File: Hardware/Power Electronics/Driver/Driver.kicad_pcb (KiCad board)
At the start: 2 copper layers, 201.5 x 165.9 mm, 48 parts

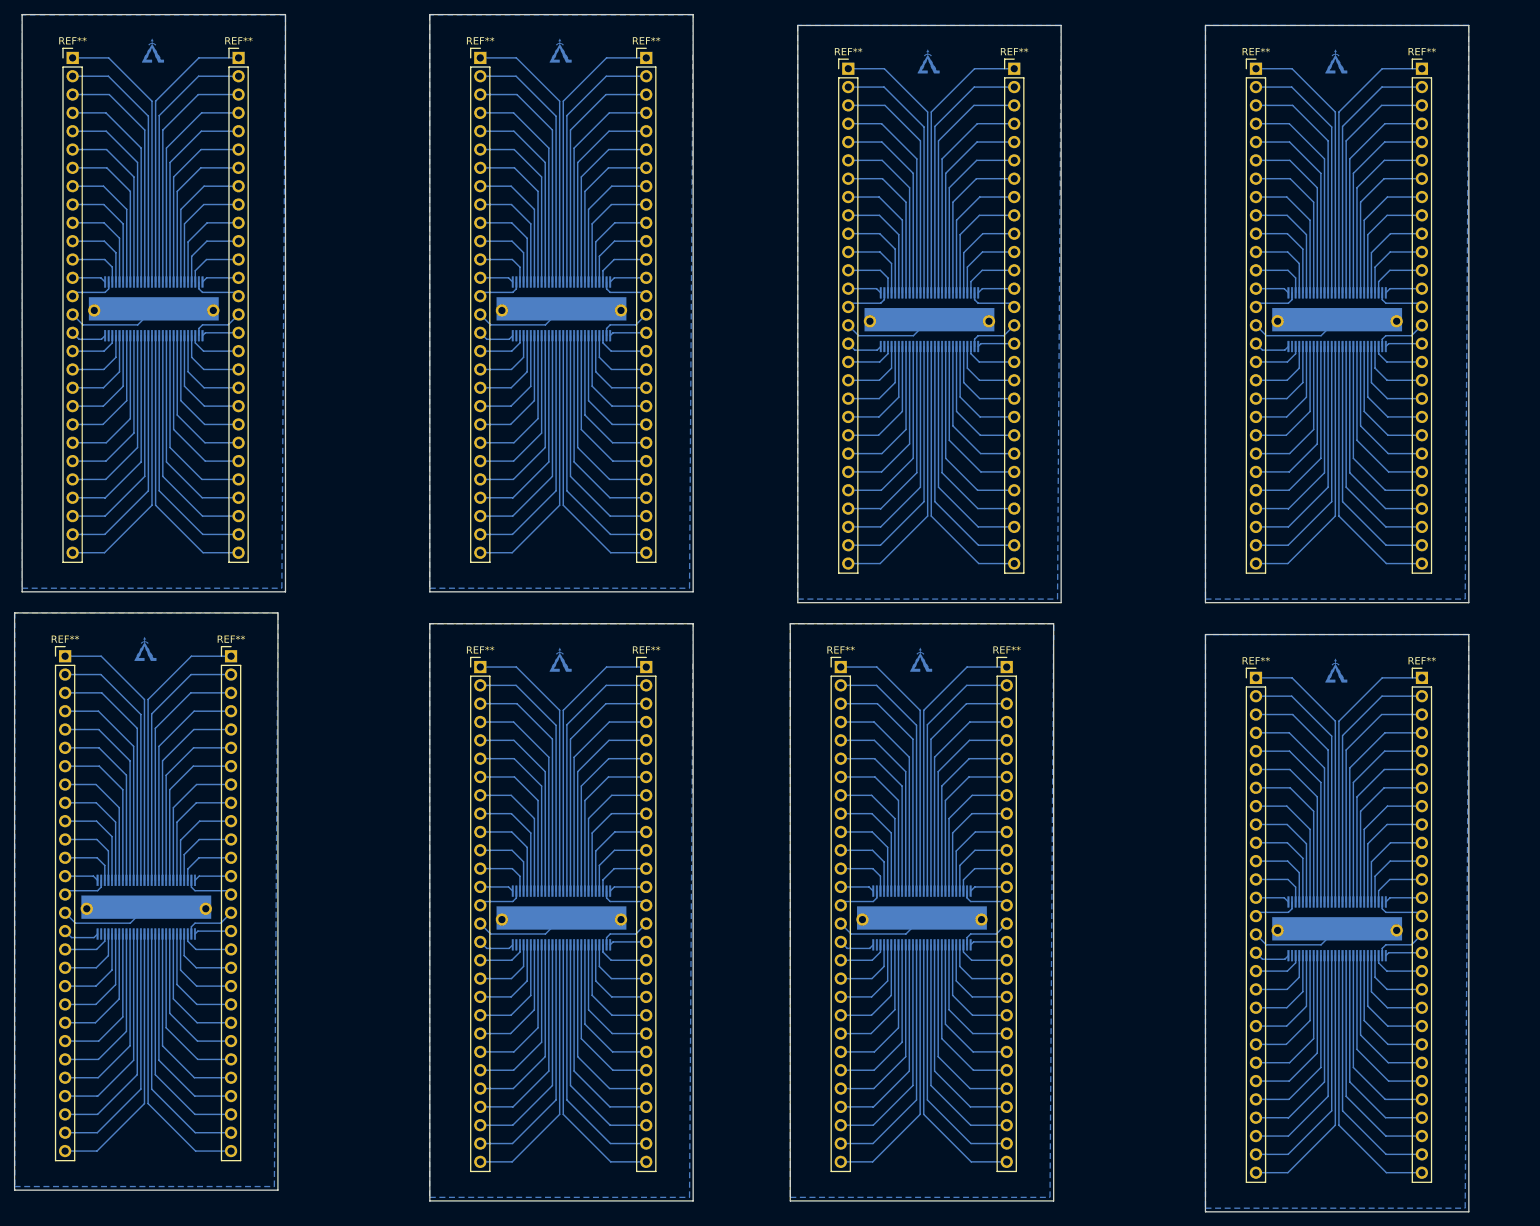
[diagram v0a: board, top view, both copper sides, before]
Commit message: fix: drv footprint correction
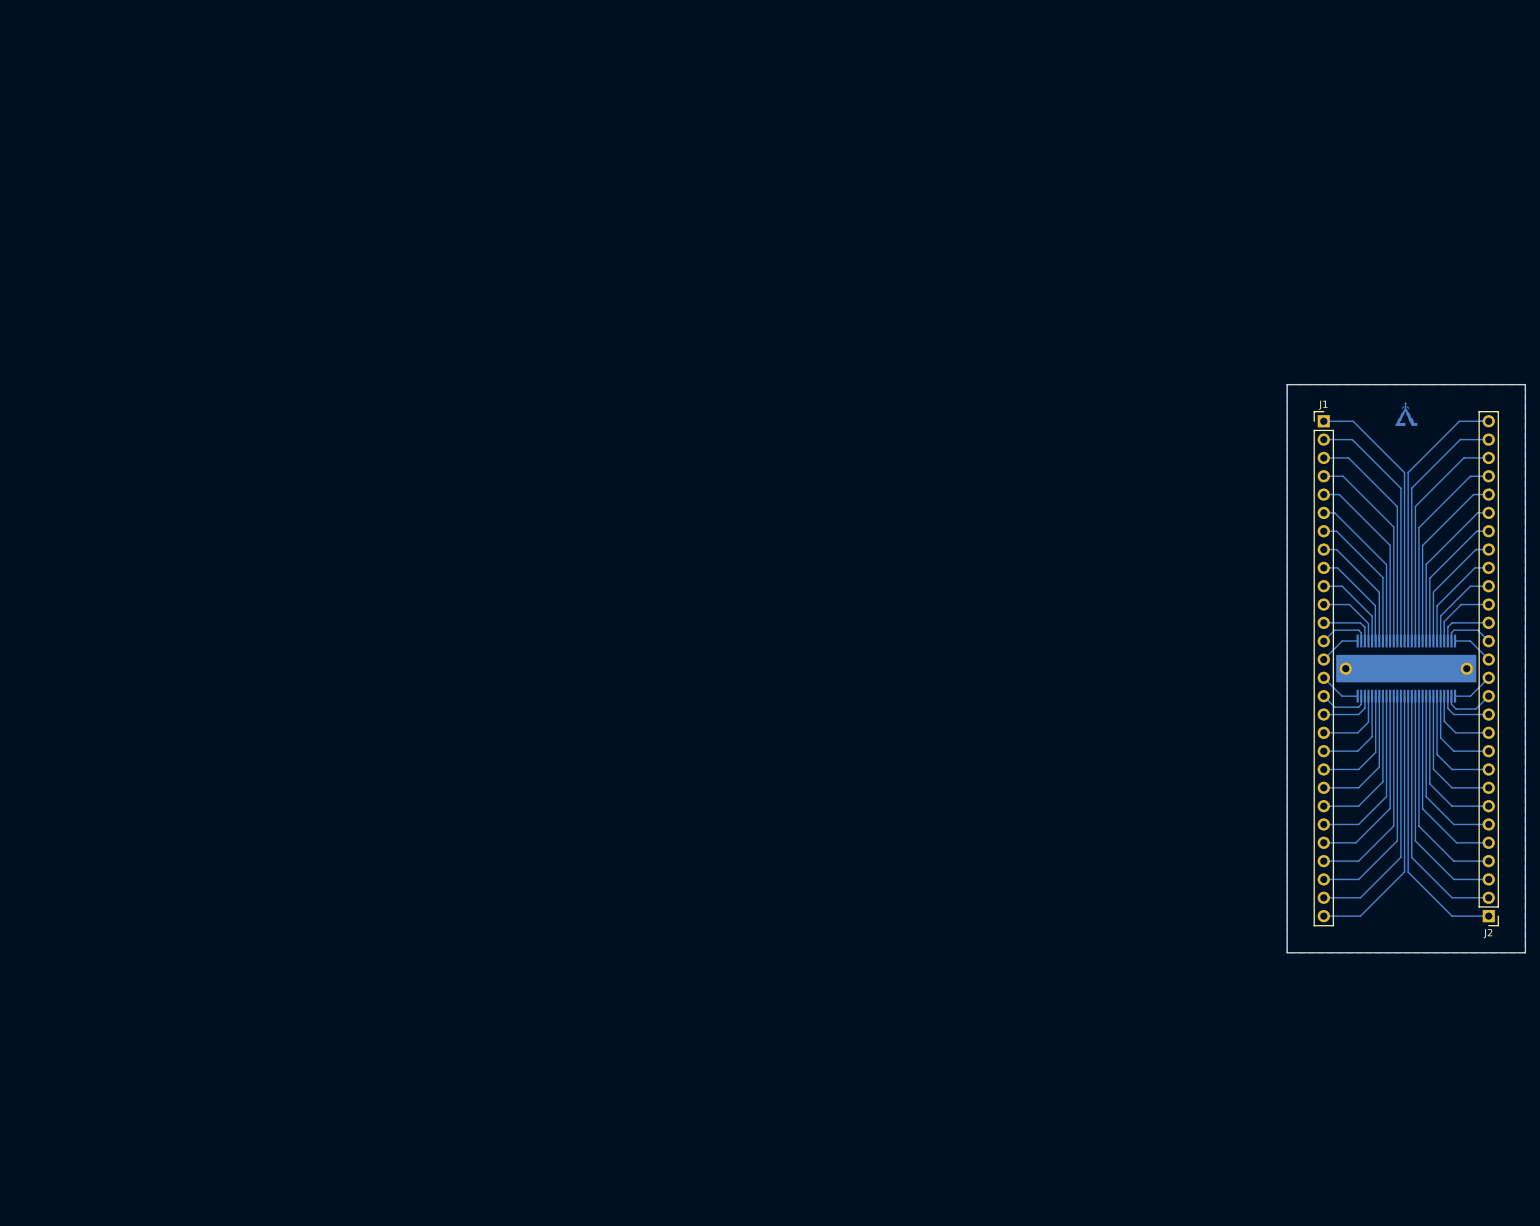
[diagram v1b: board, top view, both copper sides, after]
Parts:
- removed the ? at (151.5, 142.0)
- removed the ? at (101.5, 57.6)
- removed the ? at (85.0, 57.6)
- removed the ? at (85.0, 142.0)
- removed the ? at (209.0, 59.1)
- removed the ? at (135.0, 142.0)
- removed the ? at (101.5, 142.0)
- removed the ? at (192.5, 143.5)
- removed the ? at (27.5, 140.5)
- removed the ? at (192.5, 59.1)
- removed the ? at (44.0, 140.5)
- removed the ? at (28.5, 57.6)
- removed the ? at (209.0, 143.5)
- removed the ? at (45.0, 57.6)
- removed the ? at (136.0, 59.1)
- removed the ? at (152.5, 59.1)
- removed the G*** at (200.5, 108.0)
- removed the G*** at (143.0, 106.5)
- removed the G*** at (93.0, 106.5)
- removed the G*** at (35.5, 105.0)
- removed the G*** at (36.5, 22.1)
- removed the G*** at (144.0, 23.6)
- removed the G*** at (93.0, 22.1)
- removed the G*** at (200.5, 23.6)
- removed REF** (x16): PinHeader_1x28_P2.54mm_Vertical, Connector_PinHeader_2.54mm:PinHeader_1x28_P2.54mm_Vertical
- removed REF** (x8): SOP50P810X120-57N, drv8301car:SOP50P810X120-57N
- added ?: , , F.Cu at (218.7, 107.2)
- added ?: , , B.Cu at (201.9, 107.2)
- added G***: LOGO, imagenes:cdd, F.Cu at (210.2, 72.4)
- added J1: Conn_01x28, Connector_PinHeader_2.54mm:PinHeader_1x28_P2.54mm_Vertical, F.Cu at (198.9, 72.9)
- added J2: Conn_01x28, Connector_PinHeader_2.54mm:PinHeader_1x28_P2.54mm_Vertical, F.Cu at (221.8, 141.5)
- added U2: DRV8301DCAR, DRV8301DCAR:DRV8301DCAR PADGND, B.Cu at (210.3, 107.2)
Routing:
- net (no net): track 9288.2 -> 0.00 mm
- net BST_B: track 0.00 -> 38.6 mm
- net CP2: track 0.00 -> 38.1 mm
- net CP1: track 0.00 -> 38.1 mm
- net GH_B: track 0.00 -> 37.5 mm
- net EN_GATE: track 0.00 -> 35.3 mm
- net GVDD: track 0.00 -> 35.3 mm
- net SH_B: track 0.00 -> 34.6 mm
- net SL_A: track 0.00 -> 34.6 mm
- net INH_A: track 0.00 -> 32.5 mm
- net DC_CAL: track 0.00 -> 32.4 mm
- net GL_B: track 0.00 -> 31.6 mm
- net GL_A: track 0.00 -> 31.6 mm
- net INL_A: track 0.00 -> 29.7 mm
- net SCLK: track 0.00 -> 29.7 mm
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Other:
- board size 201.5 x 165.9 mm -> 33 x 78.7 mm
